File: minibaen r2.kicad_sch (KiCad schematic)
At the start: 134 parts, among them SW1 SW_Push, SW2 RotaryEncoder_Switch, U1 ATmega32U2-A, U2 PRTR5V0U2X, Y1 Crystal_GND24_Small

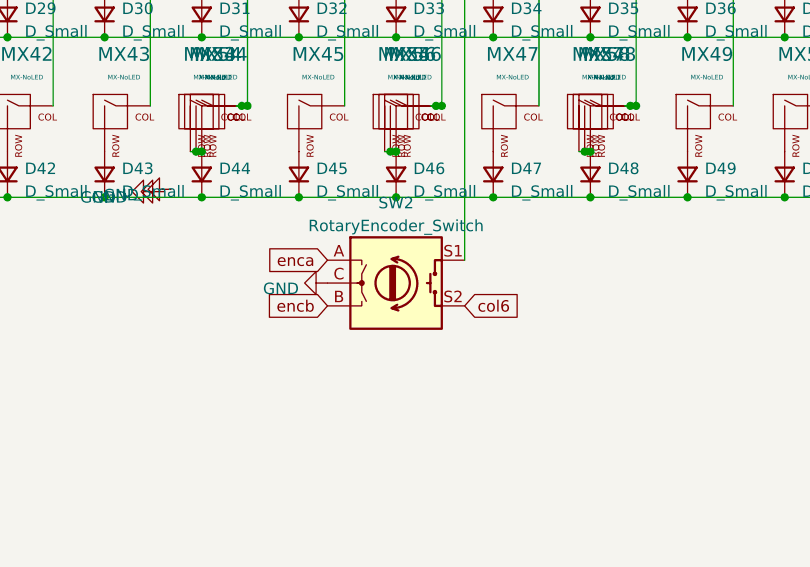
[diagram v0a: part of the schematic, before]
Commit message: Add submodules
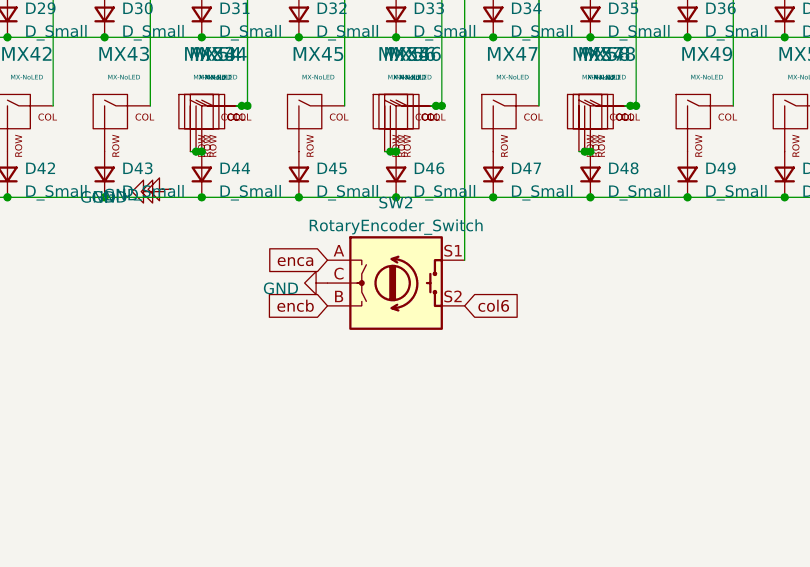
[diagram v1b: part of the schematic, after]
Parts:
- MX14, MX40: footprint MX_Only:MXOnly-1U-NoLED -> MX_Only:MXOnly-1.25U-NoLED
- MX27: footprint MX_Only:MXOnly-1U-NoLED -> MX_Only:MXOnly-1.75U-NoLED

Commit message: add
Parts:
- removed D20, D33, D44, D45, D47, D48: D_Small, Diode_SMD:D_SOD-123, symbol Device:D_Small
- removed H1, H2, H3: MountingHole, MountingHole:MountingHole_2.2mm_M2_DIN965_Pad, symbol Mechanical:MountingHole
- removed MX20, MX33, MX44, MX45, MX47: MX-NoLED, MX_Only:MXOnly-1U-NoLED, symbol keybage:MX-NoLED
- removed MX53, MX57: MX-NoLED, MX_Only:MXOnly-2U-ReversedStabilizers-NoLED, symbol keybage:MX-NoLED
- removed MX54, MX56, MX58: MX-NoLED, MX_Only:MXOnly-3U-ReversedStabilizers-NoLED, symbol keybage:MX-NoLED
- removed MX55: MX-NoLED, MX_Only:MXOnly-7U-ReversedStabilizers-NoLED, symbol keybage:MX-NoLED
- added D26, D43: D_Small, Diode_SMD:D_SOD-123, symbol Device:D_Small
- added MX26, MX40, MX41, MX42, MX43: MX-NoLED, MX_Only:MXOnly-1U-NoLED, symbol keybage:MX-NoLED
- MX25: renamed from MX26; footprint MX_Only:MXOnly-1U-NoLED -> MX_Only:MXOnly-1.5U-NoLED
- MX39: renamed from MX46; footprint MX_Only:MXOnly-1U-NoLED -> MX_Only:MXOnly-1.25U-NoLED
- MX46: renamed from MX42; footprint MX_Only:MXOnly-1U-NoLED -> MX_Only:MXOnly-1.25U-NoLED
- MX47: renamed from MX43; footprint MX_Only:MXOnly-1U-NoLED -> MX_Only:MXOnly-1.75U-NoLED
- MX48: footprint MX_Only:MXOnly-1U-NoLED -> MX_Only:MXOnly-2.25U-ReversedStabilizers-NoLED
- MX49: footprint MX_Only:MXOnly-1U-NoLED -> MX_Only:MXOnly-1.75U-NoLED
- MX50, MX52: footprint MX_Only:MXOnly-1U-NoLED -> MX_Only:MXOnly-1.25U-NoLED
- renumbered C2 to C1, C4 to C2, C5 to C4, C6 to C5, C7 to C6, C1 to C7, D21 to D20, D22 to D21, D23 to D22, D24 to D23, D25 to D24, D26 to D25, D34 to D33, D35 to D34, D36 to D35, D37 to D36, D38 to D37, D39 to D38, D40 to D39, D41 to D40, D42 to D41, D43 to D42, D46 to D44, D49 to D45, D50 to D46, D51 to D47, D52 to D48, MX21 to MX20, MX22 to MX21, MX23 to MX22, MX24 to MX23, MX25 to MX24, MX34 to MX33, MX35 to MX34, MX36 to MX35, MX37 to MX36, MX38 to MX37, MX39 to MX38, MX40 to MX44, MX41 to MX45
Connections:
- net col0: now also SW2.S2; no longer MX27.1 (COL)
- net col1: now also MX27.1 (COL), MX26.1 (COL); no longer MX28.1 (COL)
- net col10: now also MX41.1 (COL)
- net col11: now also MX42.1 (COL)
- net col12: now also MX43.1 (COL)
- net col2: now also MX28.1 (COL); no longer MX29.1 (COL)
- net col3: now also MX29.1 (COL); no longer MX30.1 (COL)
- net col4: now also MX30.1 (COL); no longer MX31.1 (COL)
- net col5: now also MX31.1 (COL), MX48.1 (COL); no longer MX32.1 (COL)
- net col6: now also MX32.1 (COL); no longer SW2.S2
- net col8: no longer MX48.1 (COL)
- net col9: now also MX40.1 (COL)
- net row2: now also D26.1 (K)
- net row3: now also D43.1 (K)
- net at D45.2 (A), MX49.2 (ROW): now also MX40.2 (ROW)
- net at MX48.2 (ROW): now also D43.2 (A)
- net at SW2.S1: now also D26.2 (A)
- net at D46.2 (A), MX50.2 (ROW): now also MX41.2 (ROW)
- net at D48.2 (A), MX52.2 (ROW): now also MX43.2 (ROW)
- net at D47.2 (A), MX51.2 (ROW): now also MX42.2 (ROW)
- net at D27.2 (A), MX27.2 (ROW): now also MX26.2 (ROW)
- no-connect marks 2 -> 4
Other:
- moved on the sheet: D27, D28, D29, D30, D31, D32, MX27, MX28, MX29, MX30, MX31, MX32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

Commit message: add
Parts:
- C7: value 4.7n -> 4.7nF
- R5, R6: value 5k1 -> 5.1k
- SW1: footprint Connector_PinHeader_2.54mm:PinHeader_1x02_P2.54mm_Vertical -> Button_Switch_SMD:SW_Push_SPST_NO_Alps_SKRK
- U1: value ATmega32U2-A -> ATmega32U4-M; footprint Package_QFP:TQFP-32_7x7mm_P0.8mm -> Package_DFN_QFN:QFN-44-1EP_7x7mm_P0.5mm_EP5.2x5.2mm
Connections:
- net col10: now also U1.10 (PD4); no longer U1.11 (PD5)
- net col12: now also U1.14 (PB0); no longer U1.10 (PD4)
- net col8: now also U1.12 (PD6); no longer U1.14 (PB0)
- net col9: now also U1.11 (PD5); no longer U1.12 (PD6)
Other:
- moved on the sheet: USB1
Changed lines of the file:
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@@
   (no_connect (at 127.635 55.88))
   (no_connect (at 280.67 64.77))
-  (no_connect (at 210.82 121.92))
-  (no_connect (at 210.82 137.16))
+  (no_connect (at 205.74 120.65))
+  (no_connect (at 205.74 135.89))
   (wire (pts (xy 227.33 118.11) (xy 229.87 118.11))
     (stroke (width 0) (type solid) (color 0 0 0 0))
@@
     (stroke (width 0) (type solid) (color 0 0 0 0))
   )
-  (wire (pts (xy 210.82 142.24) (xy 213.36 142.24))
+  (wire (pts (xy 205.74 140.97) (xy 213.36 142.24))
     (stroke (width 0) (type solid) (color 0 0 0 0))
   )
@@
     (stroke (width 0) (type solid) (color 0 0 0 0))
   )
-  (wire (pts (xy 210.82 107.95) (xy 210.82 116.84))
+  (wire (pts (xy 210.82 107.95) (xy 205.74 115.57))
     (stroke (width 0) (type solid) (color 0 0 0 0))
   )
@@
     (stroke (width 0) (type solid) (color 0 0 0 0))
   )
-  (wire (pts (xy 210.82 147.32) (xy 210.82 149.86))
+  (wire (pts (xy 205.74 146.05) (xy 210.82 149.86))
     (stroke (width 0) (type solid) (color 0 0 0 0))
   )
@@
     (stroke (width 0) (type solid) (color 0 0 0 0))
   )
-  (wire (pts (xy 210.82 119.38) (xy 212.09 119.38))
+  (wire (pts (xy 205.74 118.11) (xy 212.09 119.38))
     (stroke (width 0) (type solid) (color 0 0 0 0))
   )
@@
     (stroke (width 0) (type solid) (color 0 0 0 0))
   )
-  (wire (pts (xy 210.82 124.46) (xy 213.36 124.46))
+  (wire (pts (xy 205.74 123.19) (xy 213.36 124.46))
     (stroke (width 0) (type solid) (color 0 0 0 0))
   )
@@
     (stroke (width 0) (type solid) (color 0 0 0 0))
   )
-  (wire (pts (xy 210.82 144.78) (xy 214.63 144.78))
+  (wire (pts (xy 205.74 143.51) (xy 214.63 144.78))
     (stroke (width 0) (type solid) (color 0 0 0 0))
   )
@@
     (stroke (width 0) (type solid) (color 0 0 0 0))
   )
-  (wire (pts (xy 210.82 139.7) (xy 218.44 139.7))
+  (wire (pts (xy 205.74 138.43) (xy 218.44 139.7))
     (stroke (width 0) (type solid) (color 0 0 0 0))
   )
@@
     (stroke (width 0) (type solid) (color 0 0 0 0))
   )
-  (wire (pts (xy 210.82 127) (xy 213.36 127))
+  (wire (pts (xy 205.74 125.73) (xy 213.36 127))
     (stroke (width 0) (type solid) (color 0 0 0 0))
   )
-  (wire (pts (xy 212.09 134.62) (xy 210.82 134.62))
+  (wire (pts (xy 212.09 134.62) (xy 205.74 133.35))
     (stroke (width 0) (type solid) (color 0 0 0 0))
   )
@@
     (stroke (width 0) (type default) (color 0 0 0 0))
   )
-  (wire (pts (xy 213.36 132.08) (xy 210.82 132.08))
+  (wire (pts (xy 213.36 132.08) (xy 205.74 130.81))
     (stroke (width 0) (type solid) (color 0 0 0 0))
   )
@@
     (stroke (width 0) (type default) (color 0 0 0 0))
   )
-  (wire (pts (xy 210.82 129.54) (xy 212.09 129.54))
+  (wire (pts (xy 205.74 128.27) (xy 212.09 129.54))
     (stroke (width 0) (type solid) (color 0 0 0 0))
   )
@@
     )
   )
-  (global_label "col12" (shape input) (at 280.67 90.17 0) (fields_autoplaced)
+  (global_label "col12" (shape input) (at 280.67 41.91 0) (fields_autoplaced)
     (effects (font (size 1.27 1.27)) (justify left))
-    (property "Intersheet References" "${INTERSHEET_REFS}" (id 0) (at 288.405 90.0906 0)
+    (property "Intersheet References" "${INTERSHEET_REFS}" (id 0) (at 288.405 41.8306 0)
       (effects (font (size 1.27 1.27)) (justify left) hide)
     )
@@
     )
   )
-  (global_label "col9" (shape input) (at 280.67 95.25 0) (fields_autoplaced)
+  (global_label "col9" (shape input) (at 280.67 92.71 0) (fields_autoplaced)
     (effects (font (size 1.27 1.27)) (justify left))
-    (property "Intersheet References" "${INTERSHEET_REFS}" (id 0) (at 287.1955 95.1706 0)
+    (property "Intersheet References" "${INTERSHEET_REFS}" (id 0) (at 287.1955 92.6306 0)
       (effects (font (size 1.27 1.27)) (justify left) hide)
     )
@@
     )
   )
-  (global_label "col8" (shape input) (at 280.67 41.91 0) (fields_autoplaced)
+  (global_label "col8" (shape input) (at 280.67 95.25 0) (fields_autoplaced)
     (effects (font (size 1.27 1.27)) (justify left))
-    (property "Intersheet References" "${INTERSHEET_REFS}" (id 0) (at 287.1955 41.8306 0)
+    (property "Intersheet References" "${INTERSHEET_REFS}" (id 0) (at 287.1955 95.1706 0)
       (effects (font (size 1.27 1.27)) (justify left) hide)
     )
@@
     )
   )
-  (global_label "col10" (shape input) (at 280.67 92.71 0) (fields_autoplaced)
+  (global_label "col10" (shape input) (at 280.67 90.17 0) (fields_autoplaced)
     (effects (font (size 1.27 1.27)) (justify left))
-    (property "Intersheet References" "${INTERSHEET_REFS}" (id 0) (at 288.405 92.6306 0)
+    (property "Intersheet References" "${INTERSHEET_REFS}" (id 0) (at 288.405 90.0906 0)
       (effects (font (size 1.27 1.27)) (justify left) hide)
     )
@@
     (property "Reference" "SW1" (id 0) (at 234.95 34.671 0))
     (property "Value" "SW_Push" (id 1) (at 234.95 36.9824 0))
-    (property "Footprint" "Connector_PinHeader_2.54mm:PinHeader_1x02_P2.54mm_Vertical" (id 2) (at 234.95 36.83 0)
+    (property "Footprint" "Button_Switch_SMD:SW_Push_SPST_NO_Alps_SKRK" (id 2) (at 234.95 36.83 0)
       (effects (font (size 1.27 1.27)) hide)
     )
@@
     (pin "2")
   )
-  (symbol (lib_id "Type-C:HRO-TYPE-C-31-M-12") (at 208.28 130.81 0) (unit 1)
+  (symbol (lib_id "Type-C:HRO-TYPE-C-31-M-12") (at 203.2 129.54 0) (unit 1)
     (in_bom yes) (on_board yes)
-    (property "Reference" "USB1" (id 0) (at 204.0382 110.5662 0)
+    (property "Reference" "USB1" (id 0) (at 198.9582 109.2962 0)
       (effects (font (size 1.524 1.524)))
     )
-    (property "Value" "HRO-TYPE-C-31-M-12" (id 1) (at 204.0382 113.2586 0)
+    (property "Value" "HRO-TYPE-C-31-M-12" (id 1) (at 198.9582 111.9886 0)
       (effects (font (size 1.524 1.524)))
     )
-    (property "Footprint" "Type-C:HRO-TYPE-C-31-M-12" (id 2) (at 208.28 130.81 0)
+    (property "Footprint" "Type-C:HRO-TYPE-C-31-M-12" (id 2) (at 203.2 129.54 0)
       (effects (font (size 1.524 1.524)) hide)
     )
-    (property "Datasheet" "" (id 3) (at 208.28 130.81 0)
+    (property "Datasheet" "" (id 3) (at 203.2 129.54 0)
       (effects (font (size 1.524 1.524)) hide)
     )
@@
       (effects (font (size 1.27 1.27)) (justify right))
     )
-    (property "Value" "4.7n" (id 1) (at 186.8932 158.623 0)
+    (property "Value" "4.7nF" (id 1) (at 186.8932 158.623 0)
       (effects (font (size 1.27 1.27)) (justify right))
     )
@@
     (in_bom yes) (on_board yes)
     (property "Reference" "R5" (id 0) (at 215.9 119.4816 90))
-    (property "Value" "5k1" (id 1) (at 215.9 121.793 90))
+    (property "Value" "5.1k" (id 1) (at 215.9 121.793 90))
     (property "Footprint" "Resistor_SMD:R_0603_1608Metric" (id 2) (at 215.9 124.46 0)
       (effects (font (size 1.27 1.27)) hide)
@@
     (in_bom yes) (on_board yes)
     (property "Reference" "R6" (id 0) (at 220.98 134.7216 90))
-    (property "Value" "5k1" (id 1) (at 220.98 137.033 90))
+    (property "Value" "5.1k" (id 1) (at 220.98 137.033 90))
     (property "Footprint" "Resistor_SMD:R_0603_1608Metric" (id 2) (at 220.98 139.7 0)
       (effects (font (size 1.27 1.27)) hide)
@@
     (in_bom yes) (on_board yes) (fields_autoplaced)
     (property "Reference" "U1" (id 0) (at 262.89 107.95 0))
-    (property "Value" "ATmega32U2-A" (id 1) (at 262.89 110.49 0))
-    (property "Footprint" "Package_QFP:TQFP-32_7x7mm_P0.8mm" (id 2) (at 262.89 69.85 0)
+    (property "Value" "ATmega32U4-M" (id 1) (at 262.89 110.49 0))
+    (property "Footprint" "Package_DFN_QFN:QFN-44-1EP_7x7mm_P0.5mm_EP5.2x5.2mm" (id 2) (at 262.89 69.85 0)
       (effects (font (size 1.27 1.27) italic) hide)
     )
-    (property "Datasheet" "http://ww1.microchip.com/downloads/en/DeviceDoc/doc7799.pdf" (id 3) (at 262.89 69.85 0)
+    (property "Datasheet" "" (id 3) (at 262.89 69.85 0)
       (effects (font (size 1.27 1.27)) hide)
     )
@@
     )
     (path "/00000000-0000-0000-0000-00005fb89313"
-      (reference "C7") (unit 1) (value "4.7n") (footprint "Capacitor_SMD:C_0603_1608Metric")
+      (reference "C7") (unit 1) (value "4.7nF") (footprint "Capacitor_SMD:C_0603_1608Metric")
     )
     (path "/4096bf41-3908-453c-b16b-52b72a81b7a4"
@@
     )
     (path "/00000000-0000-0000-0000-00005fc48136"
-      (reference "R5") (unit 1) (value "5k1") (footprint "Resistor_SMD:R_0603_1608Metric")
+      (reference "R5") (unit 1) (value "5.1k") (footprint "Resistor_SMD:R_0603_1608Metric")
     )
     (path "/00000000-0000-0000-0000-00005fc49d19"
-      (reference "R6") (unit 1) (value "5k1") (footprint "Resistor_SMD:R_0603_1608Metric")
+      (reference "R6") (unit 1) (value "5.1k") (footprint "Resistor_SMD:R_0603_1608Metric")
     )
     (path "/00000000-0000-0000-0000-00005fb8883d"
@@
     )
     (path "/00000000-0000-0000-0000-00005faca656"
-      (reference "SW1") (unit 1) (value "SW_Push") (footprint "Connector_PinHeader_2.54mm:PinHeader_1x02_P2.54mm_Vertical")
+      (reference "SW1") (unit 1) (value "SW_Push") (footprint "Button_Switch_SMD:SW_Push_SPST_NO_Alps_SKRK")
     )
     (path "/29392f04-ea5c-48c3-8fe0-a41e8589c2b7"
@@
     )
     (path "/8541e986-2b2b-4942-8c66-0b6939dd52db"
-      (reference "U1") (unit 1) (value "ATmega32U2-A") (footprint "Package_QFP:TQFP-32_7x7mm_P0.8mm")
+      (reference "U1") (unit 1) (value "ATmega32U4-M") (footprint "Package_DFN_QFN:QFN-44-1EP_7x7mm_P0.5mm_EP5.2x5.2mm")
     )
     (path "/a143f620-ffcd-428f-be64-b671165c8969"
